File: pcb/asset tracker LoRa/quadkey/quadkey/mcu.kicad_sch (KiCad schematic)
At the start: 1 part

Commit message: quadkey
quadkey print klaar
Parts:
- added AE1: Antenna, vanalles:Texas_SWRA117D_2.4GHz_Right, symbol Device:Antenna
- added C10, C6, C7: 100nF, vanalles:0603, symbol Device:C_Small
- added C11, C14: NM, vanalles:0603, symbol Device:C_Small
- added C12, C13: 12pF, vanalles:0603, symbol Device:C_Small
- added C5: 4.7uF, vanalles:0603, symbol Device:C_Small
- added C8: 1uF, vanalles:0603, symbol Device:C_Small
- added C9: 100pF, vanalles:0603, symbol Device:C_Small
- added CON1: jtag, connectors_user:SAMTEC_FTSH-105-01-F-D-K, symbol conectors:jtag
- added R5: 0, vanalles:0603RL, symbol Device:R_Small_US
- added Y1: 326MhZ, vanalles:OSCCC200X160X50L55X65, symbol Device:Crystal_GND24
- U3: renamed from U?; footprint Package_DFN_QFN:QFN-48-1EP_6x6mm_P0.4mm_EP4.6x4.6mm -> halfgeleiders:nrf
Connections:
- net at U3.1 (DEC1): now also C10.2
- net +3V3: now reaches U3.13 (VDD), U3.36 (VDD), U3.48 (VDD)
- net +3V3: now also C5.2, C6.2, C7.2, CON1.1 (VCC)
- net RST: now reaches U3.24 (P0.21/~RESET)
- net RST: now also CON1.10 (tRST)
- net SWDCLK: now reaches U3.25 (SWDCLK)
- net SWDCLK: now also CON1.4 (SWDCLK/TCK)
- net SWDIO: now reaches U3.26 (SWDIO)
- net SWDIO: now also CON1.2 (SWDIO/TMS)
- net at U3.30 (ANT): now also C11.1, R5.1
- net GND: now reaches U3.31 (VSS), U3.45 (VSS), U3.49 (VSS)
- net GND: now also U3.32 (DEC2), C10.1, C11.2, C12.2, C13.2, C14.2, C5.1, C6.1, C7.1, C8.1, C9.1, CON1.3 (GND), CON1.5 (GND), CON1.9 (GND), Y1.2, Y1.4
- net at U3.33 (DEC3): now also C9.2
- net at U3.34 (XC1): now also C12.1, Y1.3
- net at U3.35 (XC2): now also C13.1, Y1.1
- net at U3.46 (DEC4): now also C8.2
- new net: AE1.1 (A), C14.1, R5.2
- no-connect marks 0 -> 35
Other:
- company: (none) -> eurocircuits 
- title: (none) -> quadkey

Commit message: 34t
34t
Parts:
- CON1: footprint connectors_user:SAMTEC_FTSH-105-01-F-D-K -> connectors_user:Tag-Connect_TC2050-IDC-FP_2x05_P1.27mm_Vertical
- Y1: footprint vanalles:OSCCC200X160X50L55X65 -> vanalles:OSCCC320X250X90L80X100N
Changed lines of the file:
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@@
       (effects (font (size 1.27 1.27)) (justify right))
     )
-    (property "Footprint" "vanalles:OSCCC200X160X50L55X65" (id 2) (at 184.15 91.44 0)
+    (property "Footprint" "vanalles:OSCCC320X250X90L80X100N" (id 2) (at 184.15 91.44 0)
       (effects (font (size 1.27 1.27)) hide)
     )
@@
     (property "Reference" "CON1" (id 0) (at 238.76 114.3 0))
     (property "Value" "jtag" (id 1) (at 238.76 116.84 0))
-    (property "Footprint" "connectors_user:SAMTEC_FTSH-105-01-F-D-K" (id 2) (at 251.46 119.38 0)
+    (property "Footprint" "connectors_user:Tag-Connect_TC2050-IDC-FP_2x05_P1.27mm_Vertical" (id 2) (at 251.46 119.38 0)
       (effects (font (size 1.27 1.27)) hide)
     )

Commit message: code
code
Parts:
- Y1: value 326MhZ -> 32MhZ
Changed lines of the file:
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@@
       (effects (font (size 1.27 1.27)) (justify right))
     )
-    (property "Value" "326MhZ" (id 1) (at 172.72 88.2649 90)
+    (property "Value" "32MhZ" (id 1) (at 172.72 88.2649 90)
       (effects (font (size 1.27 1.27)) (justify right))
     )

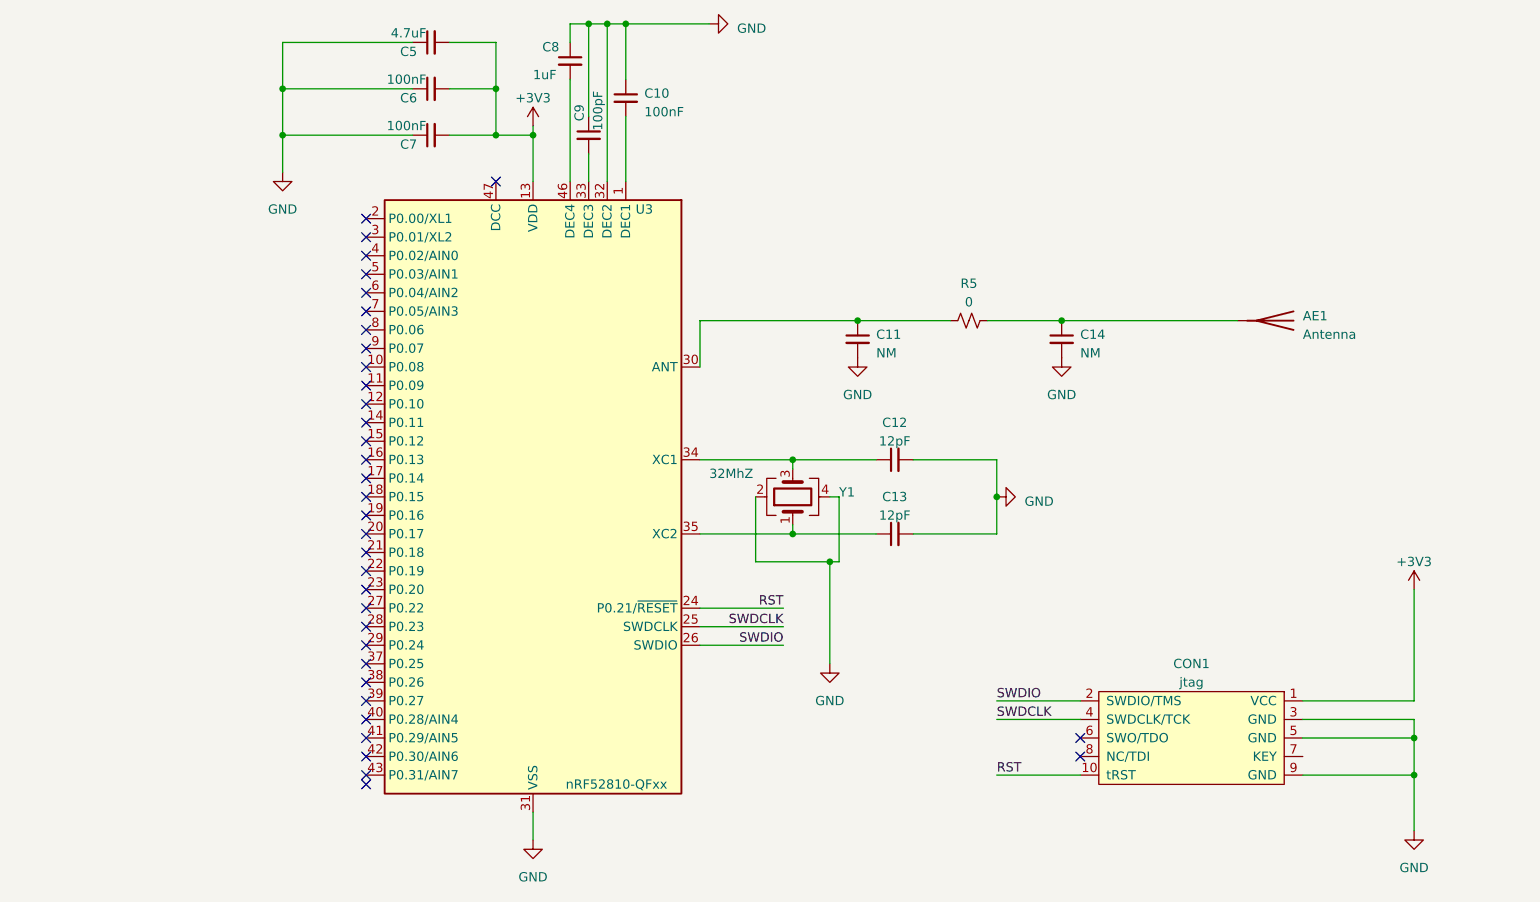
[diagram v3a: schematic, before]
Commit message: versie2
aan versie 2 begonnen met tekenen en code beginnen schrijven voor quadkey
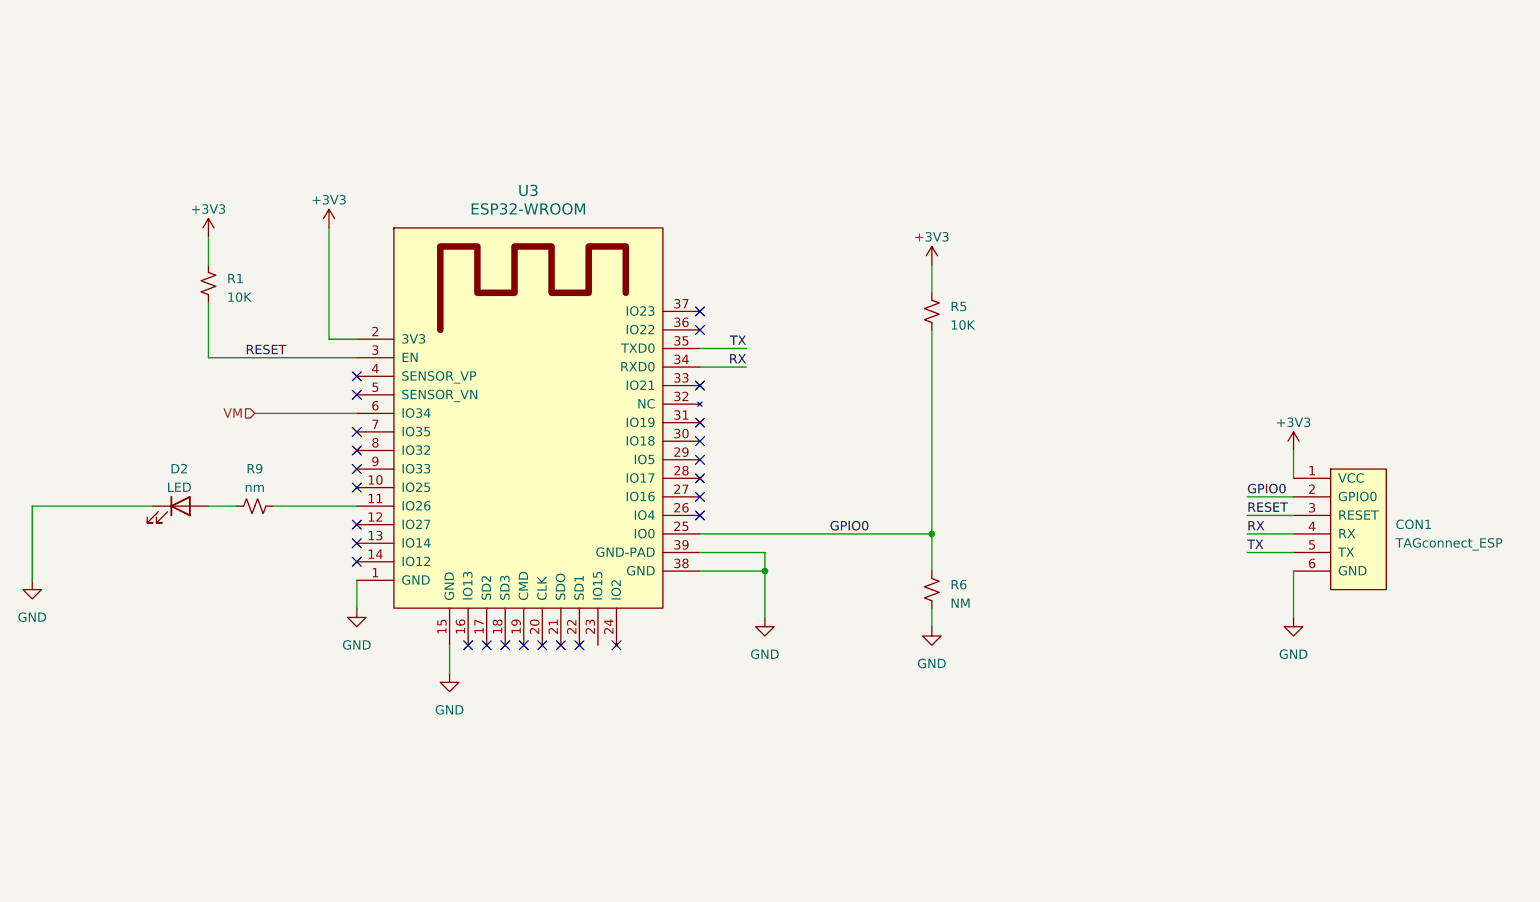
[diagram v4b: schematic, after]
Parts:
- removed AE1: Antenna, vanalles:Texas_SWRA117D_2.4GHz_Right, symbol Device:Antenna
- removed C10, C6, C7: 100nF, vanalles:0603, symbol Device:C_Small
- removed C11, C14: NM, vanalles:0603, symbol Device:C_Small
- removed C12, C13: 12pF, vanalles:0603, symbol Device:C_Small
- removed C5: 4.7uF, vanalles:0603, symbol Device:C_Small
- removed C8: 1uF, vanalles:0603, symbol Device:C_Small
- removed C9: 100pF, vanalles:0603, symbol Device:C_Small
- removed CON1: jtag, connectors_user:Tag-Connect_TC2050-IDC-FP_2x05_P1.27mm_Vertical, symbol conectors:jtag
- removed U3: nRF52810-QFxx, halfgeleiders:nrf, symbol MCU_Nordic:nRF52810-QFxx
- removed Y1: 32MhZ, vanalles:OSCCC320X250X90L80X100N, symbol Device:Crystal_GND24
- added CON1: TAGconnect_ESP, connectors_user:Tag-Connect_TC2030-IDC-NL_2x03_P1.27mm_Vertical, symbol conectors:TAGconnect_ESP
- added D2: LED, halfgeleiders:led0603, symbol Device:LED
- added R1: 10K, vanalles:0603RL, symbol Device:R_Small_US
- added R6: NM, vanalles:0603RL, symbol Device:R_Small_US
- added R9: nm, vanalles:0603RL, symbol Device:R_Small_US
- added U3: ESP32-WROOM, Module:ESP32-WROOM-32, symbol ESP32:ESP32-WROOM
- R5: value 0 -> 10K
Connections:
- net +3V3: now also R5.1, CON1.1 (VCC), R1.1, U3.2 (3V3)
- net GND: now also CON1.6 (GND), D2.1 (K), R6.2, U3.1 (GND), U3.15 (GND), U3.38 (GND), U3.39 (GND-PAD)
- net GPIO0: now reaches R5.2
- net GPIO0: now also CON1.2 (GPIO0), R6.1, U3.25 (IO0)
- new net: R9.2, U3.11 (IO26)
- new net: D2.2 (A), R9.1
- new net RESET: CON1.3 (RESET), R1.2, U3.3 (EN)
- new net RX: CON1.4 (RX), U3.34 (RXD0)
- new net TX: CON1.5 (TX), U3.35 (TXD0)
- new net VM: U3.6 (IO34)
- no-connect marks 35 -> 26
